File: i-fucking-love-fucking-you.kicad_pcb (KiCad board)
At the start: 2 copper layers, 52.7 x 197 mm, 102 parts, among them J1 Conn_01x06_Female, J2 Conn_01x05_Male, Q1 2N7000, Q2 2N7000, U1 ATtiny10-TS

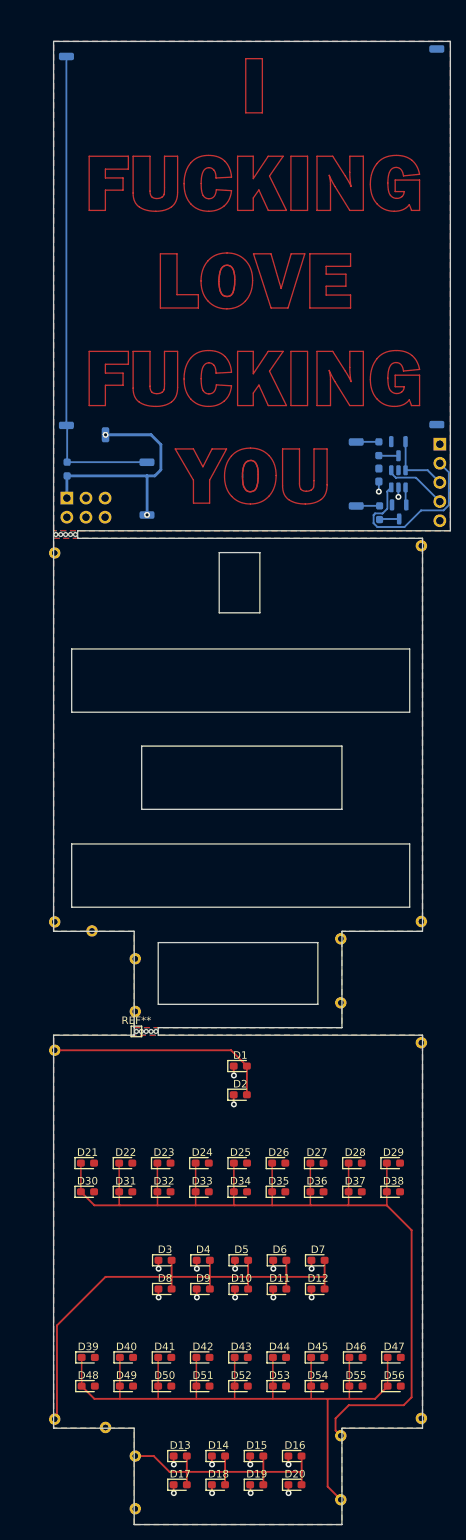
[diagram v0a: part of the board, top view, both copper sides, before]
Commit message: added code to do rand from adc on start
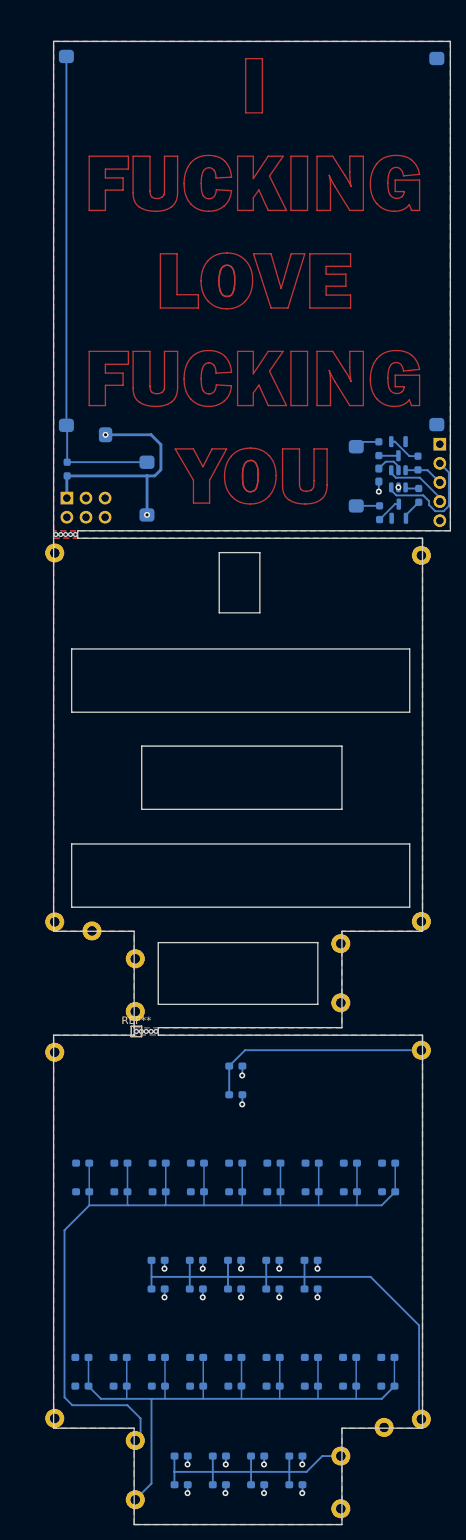
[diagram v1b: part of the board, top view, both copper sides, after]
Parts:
- added R3: 1K Ohm, Resistor_SMD:R_0603_1608Metric_Pad0.98x0.95mm_HandSolder, B.Cu at (194.0, 70.9)
- added R5: 1K Ohm, Resistor_SMD:R_0603_1608Metric_Pad0.98x0.95mm_HandSolder, B.Cu at (194.1, 75.2)
- ? (x9), D1, D10, D11, D12, D13, D14, D15, D16, D17, D18, D19, D2, D20, D21, D22, D23, D24, D25, D26, D27, D28, D29, D3, D30, D31, D32, D33, D34, D35, D36, D37, D38, D39, D4, D40, D41, D42, D43, D44, D45, D46, D47, D48, D49, D5, D50, D51, D52, D53, D54, D55, D56, D6, D7, D8, D9: moved to B.Cu
- C1: value C_Small -> .1uF
- Q1, Q2: value 2N7000 -> MMDT2222A
- R1, R2: value R_Small -> 68 Ohm
- R4: renamed from R3; value R_Small -> 68 Ohm
- moved ? 48.7 mm to (145.8, 197.8), turned to 180 degrees
- moved ? 48.7 mm to (145.8, 147.9), turned to 180 degrees
- moved ? 48.7 mm to (194.4, 197.9), turned to 180 degrees
- moved ? 48.7 mm to (194.4, 148.9), turned to 180 degrees
- moved D47 41.5 mm to (149.4, 189.7), turned to 180 degrees
- moved D56 41.5 mm to (149.4, 193.5), turned to 180 degrees
- moved D29 41.3 mm to (149.5, 163.9), turned to 180 degrees
- moved D38 41.3 mm to (149.5, 167.7), turned to 180 degrees
- moved D21 40.0 mm to (190.1, 163.9), turned to 180 degrees
- moved D30 40.0 mm to (190.1, 167.7), turned to 180 degrees
- moved D39 39.8 mm to (190.0, 189.7), turned to 180 degrees
- moved D48 39.8 mm to (190.0, 193.5), turned to 180 degrees
- moved ? 37.0 mm to (189.5, 199.0), turned to 180 degrees
- moved D46 31.3 mm to (154.4, 189.7), turned to 180 degrees
- moved D55 31.3 mm to (154.4, 193.5), turned to 180 degrees
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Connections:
- Q1 pad 2: Net-(J2-Pad3) -> Net-(Q1-Pad2)
- U1 pad 4: Net-(Q2-Pad2) -> Net-(R5-Pad2)
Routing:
- net Net-(J2-Pad2): track 23.8 -> 15.9 mm
- net Net-(Q1-Pad2): track 0.00 -> 4.62 mm
- net Net-(J2-Pad3): track 9.02 -> 5.22 mm
- net GND: track 24.5 -> 28.3 mm
- net Net-(R5-Pad2): track 0.00 -> 1.81 mm
- net VDD: track 34.8 -> 33.5 mm
- net Net-(Q2-Pad3): track 2.63 -> 3.40 mm
- net Net-(D21-Pad1): track 134.0 -> 134.6 mm
- added copper zone on F.Cu, net GND
- added copper zone on B.Cu, net VDD
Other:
- board text added: "G R C D V"
